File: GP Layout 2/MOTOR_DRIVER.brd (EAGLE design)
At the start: 91.4 x 97.5 mm, 86 parts, among them T1 2N2222, T2 2N2222, U7 ATMEGA328P_TQFP, Y1 16MHz

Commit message: added some resistors
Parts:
- removed PROGRAM: (no value), arduino_jw:CONN-2X03
- added R12, R13, R14, R15, R16: 10k, resistor:R0603
- C12, C13, C14, C15: value (none) -> 33u
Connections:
- removed net N$14: PROGRAM.5
- removed net N$15: PROGRAM.6
- net 3_3V: now also R12.1, R13.1, R14.1, R15.1
- net GND_TOP: now also R16.1
- net HALL1: now also R12.2
- net HALL1_B: now also R14.2
- net HALL2: now also R13.2
- net HALL2_B: now also R15.2
- net N$21: now also R16.2
- net SPI_MISO: no longer PROGRAM.1
- net SPI_MOSI: no longer PROGRAM.4
- net SPI_SCK: no longer PROGRAM.3
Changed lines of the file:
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@@
 <element name="BATT_LOW" library="solpad" package="SE14" value="SE14" x="6.47" y="73.71"/>
 <element name="C8" library="resistor" package="C050-025X075" value="10uF" x="46.804" y="36.508" rot="R180"/>
-<element name="C12" library="resistor" package="153CLV-1010" value="" x="6.166" y="91.8"/>
-<element name="C13" library="resistor" package="153CLV-1010" value="" x="6.258" y="81.362"/>
-<element name="C14" library="resistor" package="153CLV-1010" value="" x="6.366" y="70.5"/>
-<element name="C15" library="resistor" package="153CLV-1010" value="" x="6.166" y="58.4"/>
+<element name="C12" library="resistor" package="153CLV-1010" value="33u" x="6.166" y="91.8"/>
+<element name="C13" library="resistor" package="153CLV-1010" value="33u" x="6.258" y="81.362"/>
+<element name="C14" library="resistor" package="153CLV-1010" value="33u" x="6.366" y="70.5"/>
+<element name="C15" library="resistor" package="153CLV-1010" value="33u" x="6.166" y="58.4"/>
 <element name="FUSE" library="minifuse" package="FUSEHOLDER3588" value="" x="19.848" y="72.816"/>
 <element name="BIG_SWITCH" library="bigswitch" package="BIGSWITCH" value="" x="3.158" y="83.06" rot="R90"/>
@@
 <attribute name="MF" value="" x="52.4" y="32.4" size="1.778" layer="27" rot="R180" display="off"/>
 </element>
-<element name="PROGRAM" library="arduino_jw" package="CONN-2X03" value="" x="83" y="25.8"/>
 <element name="LED_DRIVER2" library="CSD18502KCS" package="KCS3" value="CSD18502KCS_KCS_3" x="57" y="69" rot="R90">
 <attribute name="VENDOR" value="TEXAS INSTRUMENTS" x="57" y="69" size="1.778" layer="27" rot="R90" display="off"/>
@@
 <element name="LED1_CONN2" library="con-lsta" package="FE02-1" value="" x="71" y="90" rot="R180"/>
 <element name="LED2_CONN2" library="con-lsta" package="FE02-1" value="" x="69" y="55" rot="R180"/>
+<element name="R12" library="resistor" package="R0603" value="10k" x="-30" y="-34"/>
+<element name="R13" library="resistor" package="R0603" value="10k" x="-30" y="-39"/>
+<element name="R14" library="resistor" package="R0603" value="10k" x="-30" y="-44"/>
+<element name="R15" library="resistor" package="R0603" value="10k" x="-30" y="-49"/>
+<element name="R16" library="resistor" package="R0603" value="10k" x="-30" y="-54"/>
 </elements>
 <signals>
@@
 <contactref element="U$1" pad="12/MISO"/>
 <contactref element="U7" pad="15"/>
-<contactref element="PROGRAM" pad="4"/>
 <wire x1="37.184" y1="13.698" x2="57.922" y2="17.2254" width="0" layer="19" extent="1-1"/>
-<wire x1="85.54" y1="23.26" x2="37.184" y2="13.698" width="0" layer="19" extent="1-1"/>
 </signal>
 <signal name="SPI_SCK">
 <contactref element="U7" pad="17"/>
 <contactref element="U$1" pad="13/SCK"/>
-<contactref element="PROGRAM" pad="3"/>
 <wire x1="37.184" y1="28.938" x2="60.2146" y2="18.718" width="0" layer="19" extent="1-1"/>
-<wire x1="83" y1="23.26" x2="37.184" y2="28.938" width="0" layer="19" extent="1-1"/>
 </signal>
 <signal name="SPI_MISO">
 <contactref element="U7" pad="16"/>
 <contactref element="U$1" pad="11/MOSI"/>
-<contactref element="PROGRAM" pad="1"/>
 <wire x1="34.644" y1="13.698" x2="58.722" y2="17.2254" width="0" layer="19" extent="1-1"/>
-<wire x1="83" y1="25.8" x2="34.644" y2="13.698" width="0" layer="19" extent="1-1"/>
 </signal>
 <signal name="CAMERA_SI">
@@
 <contactref element="3_3V" pad="2"/>
 <contactref element="3_3V" pad="1"/>
+<contactref element="R12" pad="1"/>
+<contactref element="R14" pad="1"/>
+<contactref element="R13" pad="1"/>
+<contactref element="R15" pad="1"/>
 <wire x1="80.586" y1="34.422" x2="77.09" y2="41.066" width="0" layer="19" extent="1-1"/>
 <wire x1="80.586" y1="30.082" x2="80.586" y2="34.422" width="0" layer="19" extent="1-1"/>
 <wire x1="72.286" y1="34.402" x2="77.09" y2="41.066" width="0" layer="19" extent="1-1"/>
 <wire x1="72.086" y1="30.162" x2="72.286" y2="34.402" width="0" layer="19" extent="1-1"/>
-<wire x1="75.682" y1="9.45" x2="80.586" y2="30.082" width="0" layer="19" extent="1-1"/>
+<wire x1="75.682" y1="9.45" x2="72.086" y2="30.162" width="0" layer="19" extent="1-1"/>
+<wire x1="75.46" y1="2" x2="75.682" y2="9.45" width="0" layer="19" extent="1-1"/>
+<wire x1="78" y1="2" x2="75.46" y2="2" width="0" layer="19" extent="1-1"/>
+<wire x1="80.54" y1="2" x2="78" y2="2" width="0" layer="19" extent="1-1"/>
+<wire x1="83.08" y1="2" x2="80.54" y2="2" width="0" layer="19" extent="1-1"/>
+<wire x1="72.92" y1="2" x2="75.46" y2="2" width="0" layer="19" extent="1-1"/>
 <wire x1="66.59" y1="9.514" x2="75.682" y2="9.45" width="0" layer="19" extent="1-1"/>
 <wire x1="9.244" y1="28.938" x2="66.59" y2="9.514" width="0" layer="19" extent="1-1"/>
-<wire x1="83.08" y1="2" x2="9.244" y2="28.938" width="0" layer="19" extent="1-1"/>
-<wire x1="80.54" y1="2" x2="83.08" y2="2" width="0" layer="19" extent="1-1"/>
-<wire x1="78" y1="2" x2="80.54" y2="2" width="0" layer="19" extent="1-1"/>
-<wire x1="75.46" y1="2" x2="78" y2="2" width="0" layer="19" extent="1-1"/>
-<wire x1="72.92" y1="2" x2="75.46" y2="2" width="0" layer="19" extent="1-1"/>
+<wire x1="-30.85" y1="-34" x2="9.244" y2="28.938" width="0" layer="19" extent="1-1"/>
+<wire x1="-30.85" y1="-39" x2="-30.85" y2="-34" width="0" layer="19" extent="1-1"/>
+<wire x1="-30.85" y1="-44" x2="-30.85" y2="-39" width="0" layer="19" extent="1-1"/>
+<wire x1="-30.85" y1="-49" x2="-30.85" y2="-44" width="0" layer="19" extent="1-1"/>
 </signal>
 <signal name="M1_GPIO1">
@@
 <contactref element="SV5" pad="3"/>
 <contactref element="SV5" pad="4"/>
+<contactref element="R16" pad="1"/>
 <wire x1="33.432" y1="94.28" x2="35.972" y2="94.28" width="0" layer="19" extent="1-1"/>
 <wire x1="20.732" y1="94.28" x2="33.432" y2="94.28" width="0" layer="19" extent="1-1"/>
@@
 <wire x1="34.245" y1="71.6757" x2="28.045" y2="71.6757" width="0" layer="19" extent="16-16"/>
 <wire x1="17.14" y1="65.64" x2="28.045" y2="71.6757" width="0" layer="19" extent="16-16"/>
+<wire x1="-30.85" y1="-54" x2="6.6" y2="55" width="0" layer="19" extent="1-1"/>
 </signal>
 <signal name="7_4V">
@@
 <contactref element="C13" pad="+"/>
 <contactref element="C14" pad="+"/>
-<wire x1="24.808" y1="75.846" x2="3.158" y2="78.41" width="0" layer="19" extent="1-1"/>
-<wire x1="24.808" y1="69.786" x2="24.808" y2="75.846" width="0" layer="19" extent="1-1"/>
-<wire x1="10.166" y1="58.4" x2="24.808" y2="75.846" width="0" layer="19" extent="1-1"/>
-<wire x1="10.366" y1="70.5" x2="10.166" y2="58.4" width="0" layer="19" extent="1-1"/>
-<wire x1="10.258" y1="81.362" x2="10.366" y2="70.5" width="0" layer="19" extent="1-1"/>
-<wire x1="10.166" y1="91.8" x2="10.258" y2="81.362" width="0" layer="19" extent="1-1"/>
+<contactref element="R16" pad="2"/>
+<wire x1="10.258" y1="81.362" x2="10.166" y2="91.8" width="0" layer="19" extent="1-1"/>
+<wire x1="3.158" y1="78.41" x2="10.258" y2="81.362" width="0" layer="19" extent="1-1"/>
+<wire x1="10.366" y1="70.5" x2="3.158" y2="78.41" width="0" layer="19" extent="1-1"/>
+<wire x1="10.166" y1="58.4" x2="10.366" y2="70.5" width="0" layer="19" extent="1-1"/>
+<wire x1="24.808" y1="69.786" x2="10.366" y2="70.5" width="0" layer="19" extent="1-1"/>
+<wire x1="24.808" y1="75.846" x2="24.808" y2="69.786" width="0" layer="19" extent="1-1"/>
+<wire x1="-29.15" y1="-54" x2="10.166" y2="58.4" width="0" layer="19" extent="1-1"/>
 </signal>
 <signal name="BATT_VOLTAGE_SENSE">
@@
 <contactref element="U7" pad="32"/>
 <contactref element="HALL1" pad="3"/>
+<contactref element="R12" pad="2"/>
 <wire x1="53.122" y1="25.8106" x2="77.366" y2="34.402" width="0" layer="19" extent="1-1"/>
+<wire x1="-29.15" y1="-34" x2="53.122" y2="25.8106" width="0" layer="19" extent="1-1"/>
 </signal>
 <signal name="CAMERA_CL">
@@
 <contactref element="HALL2" pad="3"/>
 <contactref element="U7" pad="1"/>
+<contactref element="R13" pad="2"/>
 <wire x1="51.6294" y1="24.318" x2="77.166" y2="30.162" width="0" layer="19" extent="1-1"/>
+<wire x1="-29.15" y1="-39" x2="51.6294" y2="24.318" width="0" layer="19" extent="1-1"/>
 </signal>
 <signal name="HALL1_B">
 <contactref element="HALL1_B" pad="3"/>
 <contactref element="U$1" pad="1/TX"/>
+<contactref element="R14" pad="2"/>
 <wire x1="9.244" y1="13.698" x2="85.666" y2="34.422" width="0" layer="19" extent="1-1"/>
+<wire x1="-29.15" y1="-44" x2="9.244" y2="13.698" width="0" layer="19" extent="1-1"/>
 </signal>
 <signal name="HALL2_B">
 <contactref element="HALL2_B" pad="3"/>
 <contactref element="U$1" pad="2"/>
+<contactref element="R15" pad="2"/>
 <wire x1="11.784" y1="13.698" x2="85.666" y2="30.082" width="0" layer="19" extent="1-1"/>
+<wire x1="-29.15" y1="-49" x2="11.784" y2="13.698" width="0" layer="19" extent="1-1"/>
 </signal>
 <signal name="REC_EXTRA1">
@@
 <wire x1="29.564" y1="28.938" x2="11.95" y2="24" width="0" layer="19" extent="1-1"/>
 </signal>
-<signal name="N$14">
-<contactref element="PROGRAM" pad="5"/>
-</signal>
-<signal name="N$15">
-<contactref element="PROGRAM" pad="6"/>
-</signal>
 <signal name="N$1">

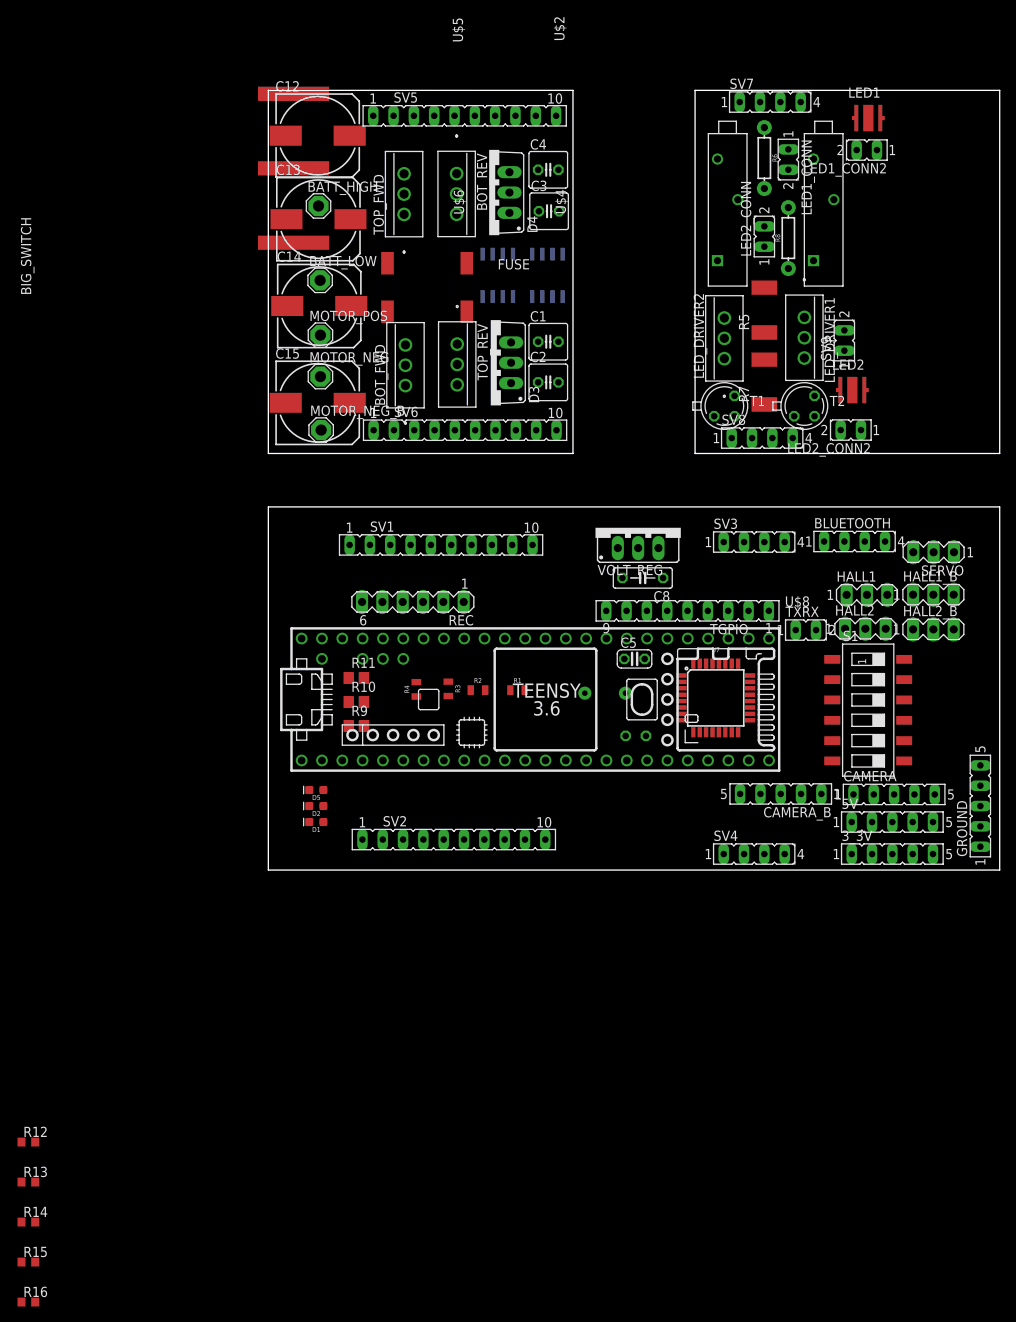
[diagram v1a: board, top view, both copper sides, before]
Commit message: added some resistors, atmega gpio, placed them
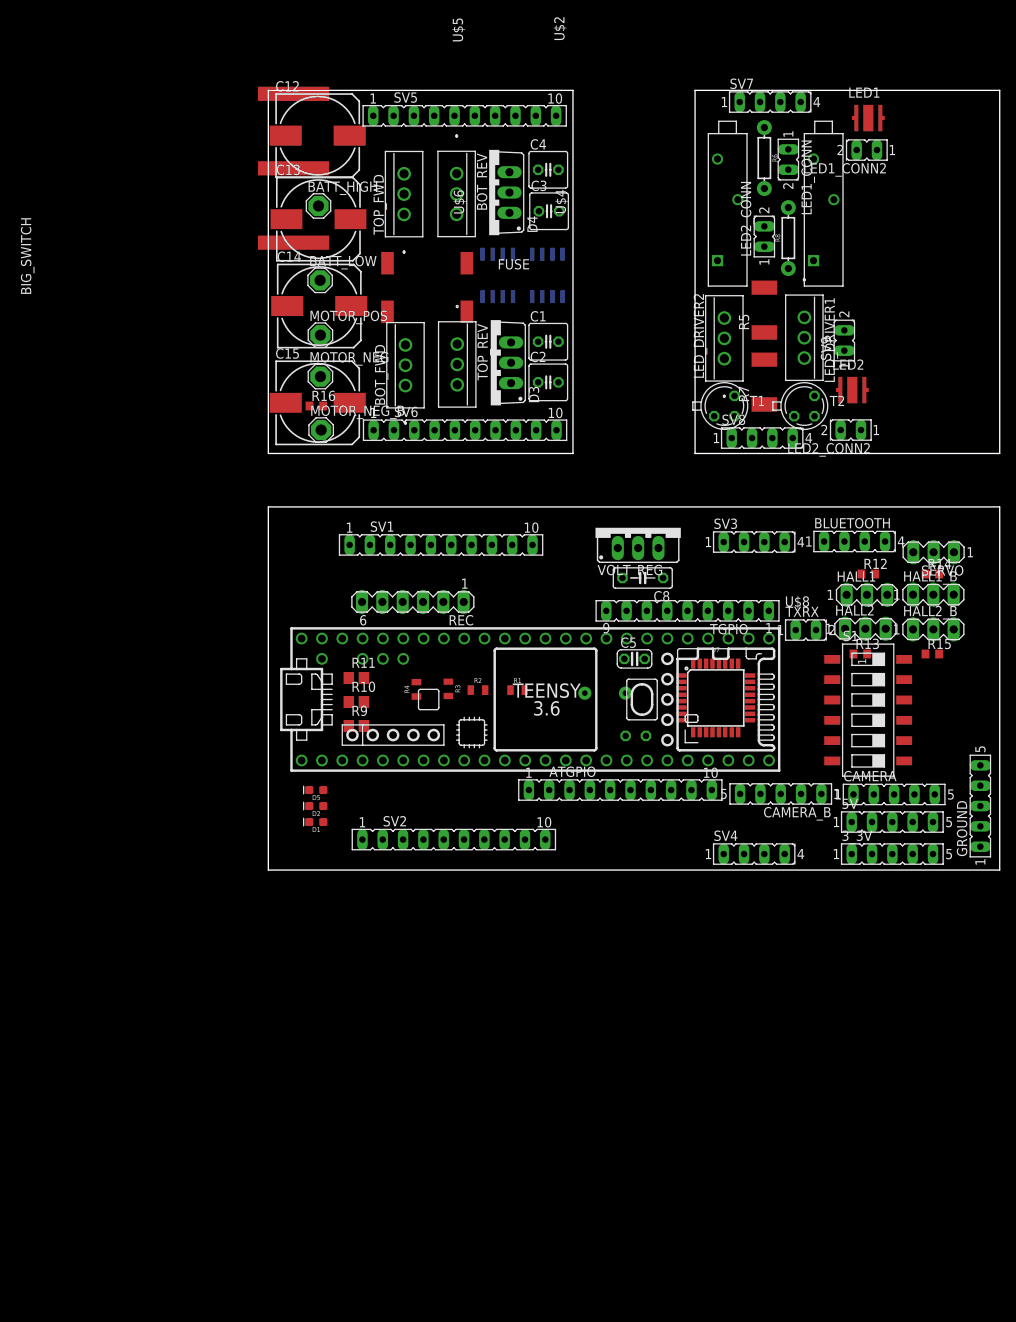
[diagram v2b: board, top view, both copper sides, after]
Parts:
- added ATGPIO: (no value), con-lsta:FE10
- moved R14 139.0 mm to (83.0, 37.0)
- moved R15 136.2 mm to (83.0, 27.0)
- moved R12 126.8 mm to (75.0, 37.0)
- moved R13 123.2 mm to (74.0, 27.0)
- moved R16 117.6 mm to (6.00, 58.0)
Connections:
- removed net M1_GPIO1: U7.27
- removed net M1_GPIO2: U7.28
- removed net M1_GPIO3: U7.13
- new net ADC6: ATGPIO.6, U7.19
- new net ADC7: ATGPIO.7, U7.22
- new net PB1: ATGPIO.10, U7.13
- new net PC1: ATGPIO.1, U7.24
- new net PC2: ATGPIO.2, U7.25
- new net PC3: ATGPIO.3, U7.26
- new net PC4: ATGPIO.4, U7.27
- new net PC5: ATGPIO.5, U7.28
- new net PD4: ATGPIO.8, U7.2
- new net PD5: ATGPIO.9, U7.9
- new net PD6: U7.10
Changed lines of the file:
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@@
 <element name="LED1_CONN2" library="con-lsta" package="FE02-1" value="" x="71" y="90" rot="R180"/>
 <element name="LED2_CONN2" library="con-lsta" package="FE02-1" value="" x="69" y="55" rot="R180"/>
-<element name="R12" library="resistor" package="R0603" value="10k" x="-30" y="-34"/>
-<element name="R13" library="resistor" package="R0603" value="10k" x="-30" y="-39"/>
-<element name="R14" library="resistor" package="R0603" value="10k" x="-30" y="-44"/>
-<element name="R15" library="resistor" package="R0603" value="10k" x="-30" y="-49"/>
-<element name="R16" library="resistor" package="R0603" value="10k" x="-30" y="-54"/>
+<element name="R12" library="resistor" package="R0603" value="10k" x="75" y="37"/>
+<element name="R13" library="resistor" package="R0603" value="10k" x="74" y="27"/>
+<element name="R14" library="resistor" package="R0603" value="10k" x="83" y="37"/>
+<element name="R15" library="resistor" package="R0603" value="10k" x="83" y="27"/>
+<element name="R16" library="resistor" package="R0603" value="10k" x="6" y="58"/>
+<element name="ATGPIO" library="con-lsta" package="FE10" value="" x="44" y="10">
+<attribute name="OC_FARNELL" value="unknown" x="44" y="10" size="1.778" layer="27" display="off"/>
+<attribute name="MF" value="" x="44" y="10" size="1.778" layer="27" display="off"/>
+<attribute name="MPN" value="" x="44" y="10" size="1.778" layer="27" display="off"/>
+<attribute name="OC_NEWARK" value="unknown" x="44" y="10" size="1.778" layer="27" display="off"/>
+</element>
 </elements>
 <signals>
@@
 <wire x1="66.59" y1="9.514" x2="75.682" y2="9.45" width="0" layer="19" extent="1-1"/>
 <wire x1="9.244" y1="28.938" x2="66.59" y2="9.514" width="0" layer="19" extent="1-1"/>
-<wire x1="-30.85" y1="-34" x2="9.244" y2="28.938" width="0" layer="19" extent="1-1"/>
-<wire x1="-30.85" y1="-39" x2="-30.85" y2="-34" width="0" layer="19" extent="1-1"/>
-<wire x1="-30.85" y1="-44" x2="-30.85" y2="-39" width="0" layer="19" extent="1-1"/>
-<wire x1="-30.85" y1="-49" x2="-30.85" y2="-44" width="0" layer="19" extent="1-1"/>
-</signal>
-<signal name="M1_GPIO1">
+<wire x1="74.15" y1="37" x2="9.244" y2="28.938" width="0" layer="19" extent="1-1"/>
+<wire x1="73.15" y1="27" x2="74.15" y2="37" width="0" layer="19" extent="1-1"/>
+<wire x1="82.15" y1="37" x2="73.15" y2="27" width="0" layer="19" extent="1-1"/>
+<wire x1="82.15" y1="27" x2="82.15" y2="37" width="0" layer="19" extent="1-1"/>
+</signal>
+<signal name="PC4">
 <contactref element="U7" pad="27"/>
-</signal>
-<signal name="M1_GPIO2">
+<contactref element="ATGPIO" pad="4"/>
+<wire x1="40.19" y1="10" x2="57.122" y2="25.8106" width="0" layer="19" extent="1-1"/>
+</signal>
+<signal name="PC5">
 <contactref element="U7" pad="28"/>
-</signal>
-<signal name="M1_GPIO3">
+<contactref element="ATGPIO" pad="5"/>
+<wire x1="42.73" y1="10" x2="56.322" y2="25.8106" width="0" layer="19" extent="1-1"/>
+</signal>
+<signal name="PB1">
 <contactref element="U7" pad="13"/>
+<contactref element="ATGPIO" pad="10"/>
+<wire x1="55.43" y1="10" x2="56.322" y2="17.2254" width="0" layer="19" extent="1-1"/>
 </signal>
 <signal name="REC_MOTOR">
@@
 <wire x1="34.245" y1="71.6757" x2="28.045" y2="71.6757" width="0" layer="19" extent="16-16"/>
 <wire x1="17.14" y1="65.64" x2="28.045" y2="71.6757" width="0" layer="19" extent="16-16"/>
-<wire x1="-30.85" y1="-54" x2="6.6" y2="55" width="0" layer="19" extent="1-1"/>
+<wire x1="5.15" y1="58" x2="6.6" y2="55" width="0" layer="19" extent="1-1"/>
 </signal>
 <signal name="7_4V">
@@
 <wire x1="24.808" y1="69.786" x2="10.366" y2="70.5" width="0" layer="19" extent="1-1"/>
 <wire x1="24.808" y1="75.846" x2="24.808" y2="69.786" width="0" layer="19" extent="1-1"/>
-<wire x1="-29.15" y1="-54" x2="10.166" y2="58.4" width="0" layer="19" extent="1-1"/>
+<wire x1="6.85" y1="58" x2="10.166" y2="58.4" width="0" layer="19" extent="1-1"/>
 </signal>
 <signal name="BATT_VOLTAGE_SENSE">
@@
 <contactref element="R12" pad="2"/>
 <wire x1="53.122" y1="25.8106" x2="77.366" y2="34.402" width="0" layer="19" extent="1-1"/>
-<wire x1="-29.15" y1="-34" x2="53.122" y2="25.8106" width="0" layer="19" extent="1-1"/>
+<wire x1="75.85" y1="37" x2="53.122" y2="25.8106" width="0" layer="19" extent="1-1"/>
 </signal>
 <signal name="CAMERA_CL">
@@
 <contactref element="R13" pad="2"/>
 <wire x1="51.6294" y1="24.318" x2="77.166" y2="30.162" width="0" layer="19" extent="1-1"/>
-<wire x1="-29.15" y1="-39" x2="51.6294" y2="24.318" width="0" layer="19" extent="1-1"/>
+<wire x1="74.85" y1="27" x2="51.6294" y2="24.318" width="0" layer="19" extent="1-1"/>
 </signal>
 <signal name="HALL1_B">
@@
 <contactref element="R14" pad="2"/>
 <wire x1="9.244" y1="13.698" x2="85.666" y2="34.422" width="0" layer="19" extent="1-1"/>
-<wire x1="-29.15" y1="-44" x2="9.244" y2="13.698" width="0" layer="19" extent="1-1"/>
+<wire x1="83.85" y1="37" x2="9.244" y2="13.698" width="0" layer="19" extent="1-1"/>
 </signal>
 <signal name="HALL2_B">
@@
 <contactref element="R15" pad="2"/>
 <wire x1="11.784" y1="13.698" x2="85.666" y2="30.082" width="0" layer="19" extent="1-1"/>
-<wire x1="-29.15" y1="-49" x2="11.784" y2="13.698" width="0" layer="19" extent="1-1"/>
+<wire x1="83.85" y1="27" x2="11.784" y2="13.698" width="0" layer="19" extent="1-1"/>
 </signal>
 <signal name="REC_EXTRA1">
@@
 <wire x1="74.5" y1="60" x2="74.85" y2="60" width="0" layer="19" extent="1-1"/>
 </signal>
+<signal name="PC1">
+<contactref element="U7" pad="24"/>
+<contactref element="ATGPIO" pad="1"/>
+<wire x1="60.2146" y1="24.318" x2="32.57" y2="10" width="0" layer="19" extent="1-1"/>
+</signal>
+<signal name="PC2">
+<contactref element="U7" pad="25"/>
+<contactref element="ATGPIO" pad="2"/>
+<wire x1="35.11" y1="10" x2="58.722" y2="25.8106" width="0" layer="19" extent="1-1"/>
+</signal>
+<signal name="PC3">
+<contactref element="U7" pad="26"/>
+<contactref element="ATGPIO" pad="3"/>
+<wire x1="37.65" y1="10" x2="57.922" y2="25.8106" width="0" layer="19" extent="1-1"/>
+</signal>
+<signal name="ADC6">
+<contactref element="U7" pad="19"/>
+<contactref element="ATGPIO" pad="6"/>
+<wire x1="45.27" y1="10" x2="60.2146" y2="20.318" width="0" layer="19" extent="1-1"/>
+</signal>
+<signal name="ADC7">
+<contactref element="U7" pad="22"/>
+<contactref element="ATGPIO" pad="7"/>
+<wire x1="47.81" y1="10" x2="60.2146" y2="22.718" width="0" layer="19" extent="1-1"/>
+</signal>
+<signal name="PD4">
+<contactref element="U7" pad="2"/>
+<contactref element="ATGPIO" pad="8"/>
+<wire x1="50.35" y1="10" x2="51.6294" y2="23.518" width="0" layer="19" extent="1-1"/>
+</signal>
+<signal name="PD5">
+<contactref element="U7" pad="9"/>
+<contactref element="ATGPIO" pad="9"/>
+<wire x1="52.89" y1="10" x2="53.122" y2="17.2254" width="0" layer="19" extent="1-1"/>
+</signal>
+<signal name="PD6">
+<contactref element="U7" pad="10"/>
+</signal>
 </signals>
